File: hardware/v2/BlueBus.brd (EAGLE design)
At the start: 95 x 65 mm, 136 parts, among them J1 3PIN_953442_1, J2 6PIN_953442_1, J3 6PIN_5_103166_1, J4 SJ2-35853A-SMT-TR, J5 SMB_CONN, J6 USB3080-30-01-A, J7 PCM12SMTR, J8 TC2030, Q1 NMOSFET-BSS138K, Q2 PMOSFET-DMP32D4SSOT323, Q3 NMOSFET-BSS138K, U1 MPQ4420, U10 PCM5122, U11 PAM8406, U2 TH3122.4, U3 FT231XS, U4 S-1212BC0-U5T1U, U5 XC6210, U6 CAT25M01, U7 PIC24FJ1024GA606, U8 BM83SM1, U9 DIT4096

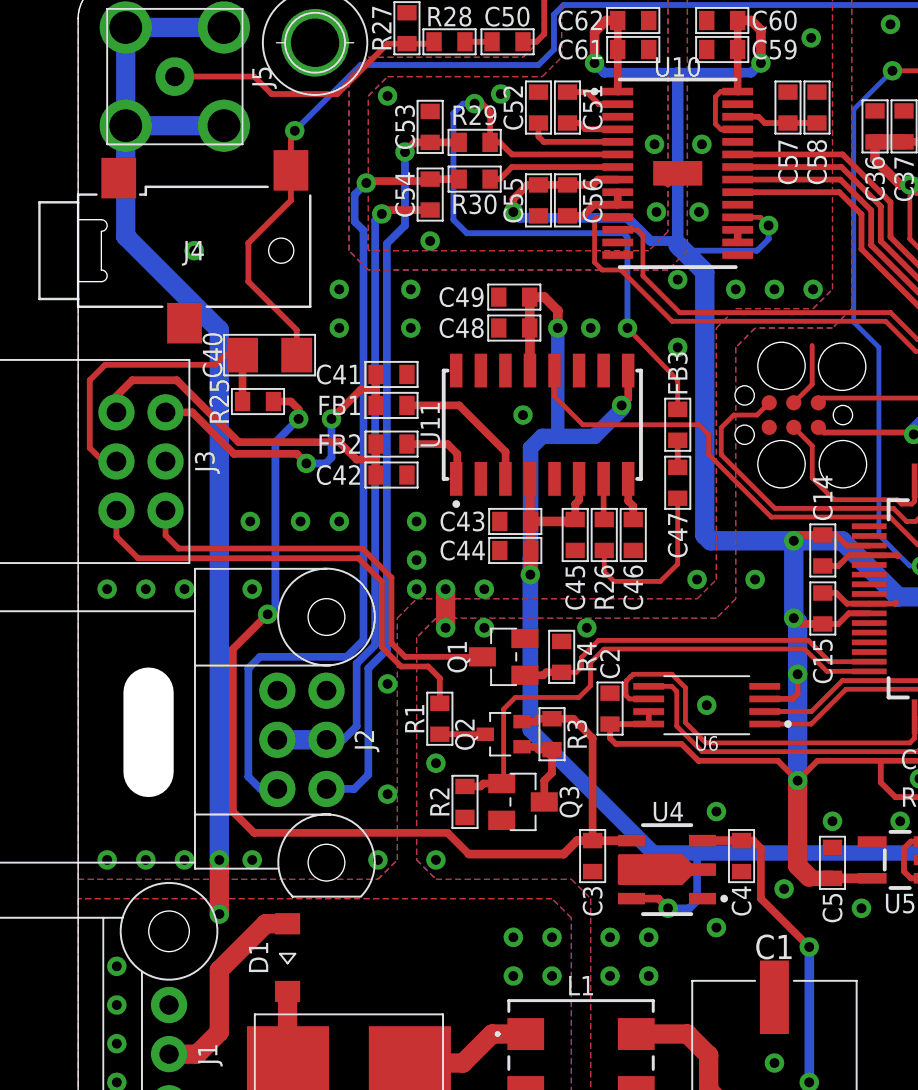
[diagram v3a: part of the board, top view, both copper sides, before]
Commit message: [IMP] hardware: V2 wiring and names * Update GND_FLT trace routing away from board cutout * Fix >NAME for some parts
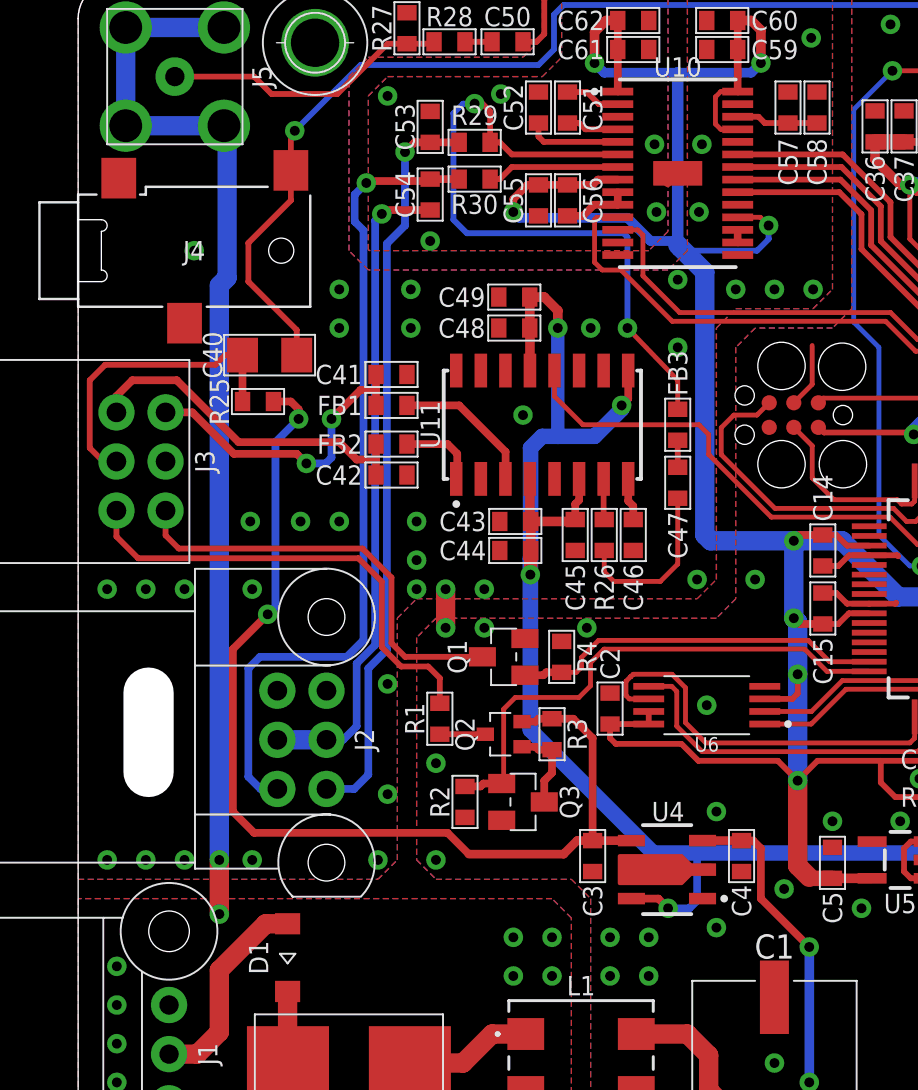
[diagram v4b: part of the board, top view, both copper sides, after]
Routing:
- net GND_FLT: track 58.0 -> 56.2 mm
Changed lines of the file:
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@@
 <element name="C1" library="Passives" package="RHS1V101MCN1GS" value="RHS1V101MCN1GS" x="36" y="9" smashed="yes" rot="R90">
 <attribute name="MFG" value="Nichicon" x="90.61" y="26.78" size="1.778" layer="27" rot="R90" display="off"/>
-<attribute name="NAME" x="36" y="15" size="1.25" layer="25" font="vector" ratio="15" rot="SR0" align="center"/>
+<attribute name="NAME" x="36" y="14.4" size="1.25" layer="25" font="vector" ratio="15" rot="SR0" align="bottom-center"/>
 <attribute name="PN" value="RHS1V101MCN1GS" x="90.61" y="26.78" size="1.778" layer="27" rot="R90" display="off"/>
 </element>
@@
 <element name="U6" library="ICs" package="TSSOP-8" value="CAT25M01" x="32.5" y="27.5" smashed="yes" rot="R180">
 <attribute name="MFG" value="ONSEMI" x="32.5" y="27.5" size="1.778" layer="27" rot="R180" display="off"/>
-<attribute name="NAME" x="32.5" y="25.9" size="0.75" layer="21" font="vector" ratio="15" rot="R180" align="bottom-center"/>
+<attribute name="NAME" x="32.5" y="25.85" size="0.75" layer="21" font="vector" ratio="15" rot="R180" align="bottom-center"/>
 <attribute name="PN" value="CAT25M01YI-GT3" x="32.5" y="27.5" size="1.778" layer="27" rot="R180" display="off"/>
 </element>
@@
 <wire x1="2.46" y1="62.54" x2="2.46" y2="57.46" width="1" layer="16"/>
 <wire x1="2.46" y1="57.46" x2="7.54" y2="57.46" width="1" layer="16"/>
-<wire x1="2.46" y1="57.46" x2="2.46" y2="51.74" width="1" layer="16"/>
-<wire x1="2.46" y1="51.74" x2="7.3" y2="46.9" width="1" layer="16"/>
 <via x="7.3" y="19.5" extent="1-16" drill="0.51"/>
-<wire x1="7.3" y1="46.9" x2="7.3" y2="19.5" width="1" layer="16"/>
 <via x="7.3" y="16.7" extent="1-16" drill="0.51"/>
 <wire x1="7.3" y1="19.5" x2="7.3" y2="16.7" width="1" layer="1"/>
+<wire x1="7.3" y1="49.2" x2="7.7" y2="49.6" width="1" layer="16"/>
+<wire x1="7.7" y1="49.6" x2="7.7" y2="57.3" width="1" layer="16"/>
+<wire x1="7.7" y1="57.3" x2="7.54" y2="57.46" width="1" layer="16"/>
+<wire x1="7.3" y1="19.5" x2="7.3" y2="49.2" width="1" layer="16"/>
+<wire x1="22.5" y1="15.5" x2="24.5" y2="15.5" width="0" layer="19" extent="1-1"/>
+<wire x1="24.5" y1="13.5" x2="24.5" y2="15.5" width="0" layer="19" extent="1-1"/>
+<wire x1="22.5" y1="13.5" x2="22.5" y2="15.5" width="0" layer="19" extent="1-1"/>
+<wire x1="23.1425" y1="7.5" x2="22.5" y2="13.5" width="0" layer="19" extent="1-1"/>
+<wire x1="22.5" y1="5" x2="23.1425" y2="7.5" width="0" layer="19" extent="1-1"/>
+<wire x1="22.5" y1="3.2" x2="22.5" y2="5" width="0" layer="19" extent="1-1"/>
+<wire x1="24.5" y1="5" x2="22.5" y2="5" width="0" layer="19" extent="1-1"/>
+<wire x1="24.5" y1="3.2" x2="24.5" y2="5" width="0" layer="19" extent="1-1"/>
+<wire x1="24.5" y1="1" x2="24.5" y2="3.2" width="0" layer="19" extent="1-1"/>
+<wire x1="22.5" y1="1" x2="24.5" y2="1" width="0" layer="19" extent="1-1"/>
+<wire x1="12.25" y1="3.25" x2="22.5" y2="3.2" width="0" layer="19" extent="1-1"/>
+<wire x1="2" y1="6" x2="12.25" y2="3.25" width="0" layer="19" extent="1-1"/>
+<wire x1="2" y1="8" x2="2" y2="6" width="0" layer="19" extent="1-1"/>
+<wire x1="2" y1="10" x2="2" y2="8" width="0" layer="19" extent="1-1"/>
+<wire x1="2" y1="12" x2="2" y2="10" width="0" layer="19" extent="1-1"/>
+<wire x1="2" y1="14" x2="2" y2="12" width="0" layer="19" extent="1-1"/>
+<wire x1="4.7" y1="12" x2="2" y2="12" width="0" layer="19" extent="1-1"/>
+<wire x1="7.3" y1="16.7" x2="4.7" y2="12" width="0" layer="19" extent="1-1"/>
 </signal>
 <signal name="MCU_VER">

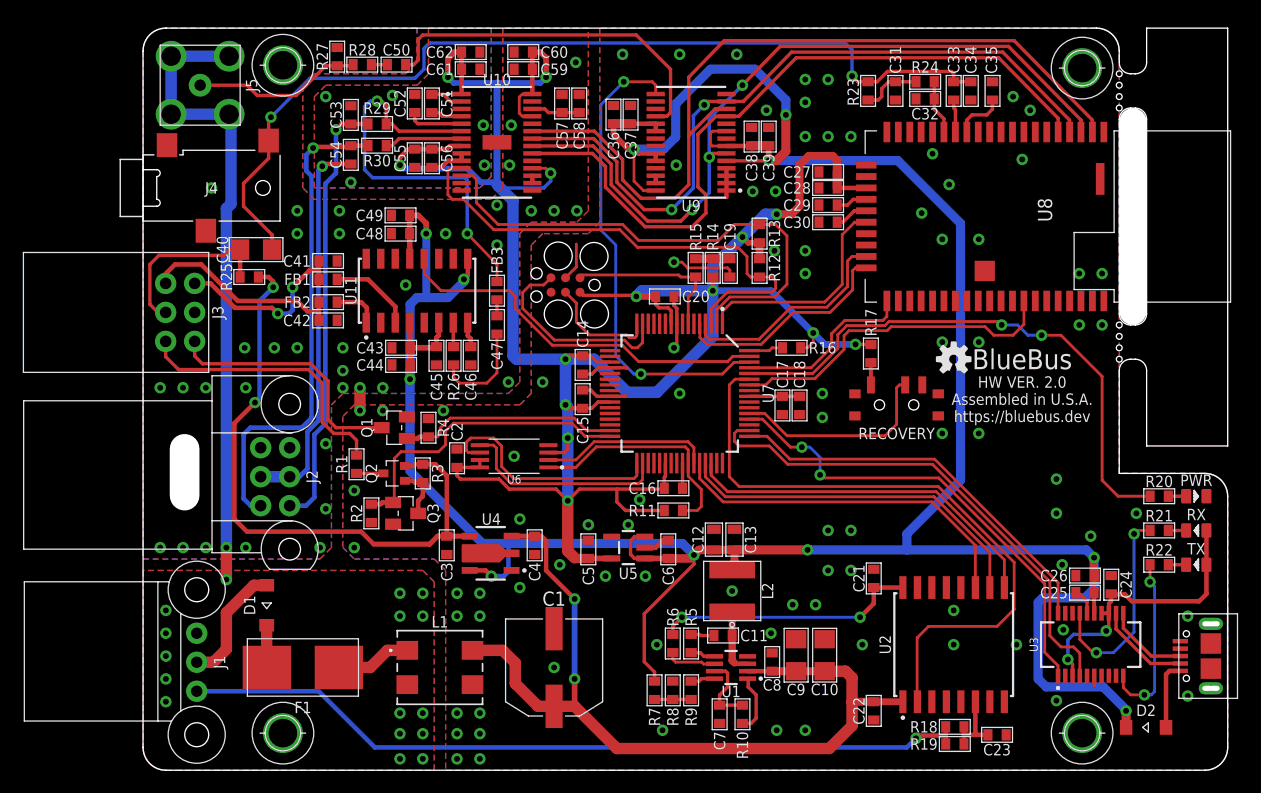
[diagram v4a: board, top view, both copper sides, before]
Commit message: [IMP] hardware: v2.0 TEL Circuit * Add Series resistor and move MOSFETs and resistors around to support BJT usage
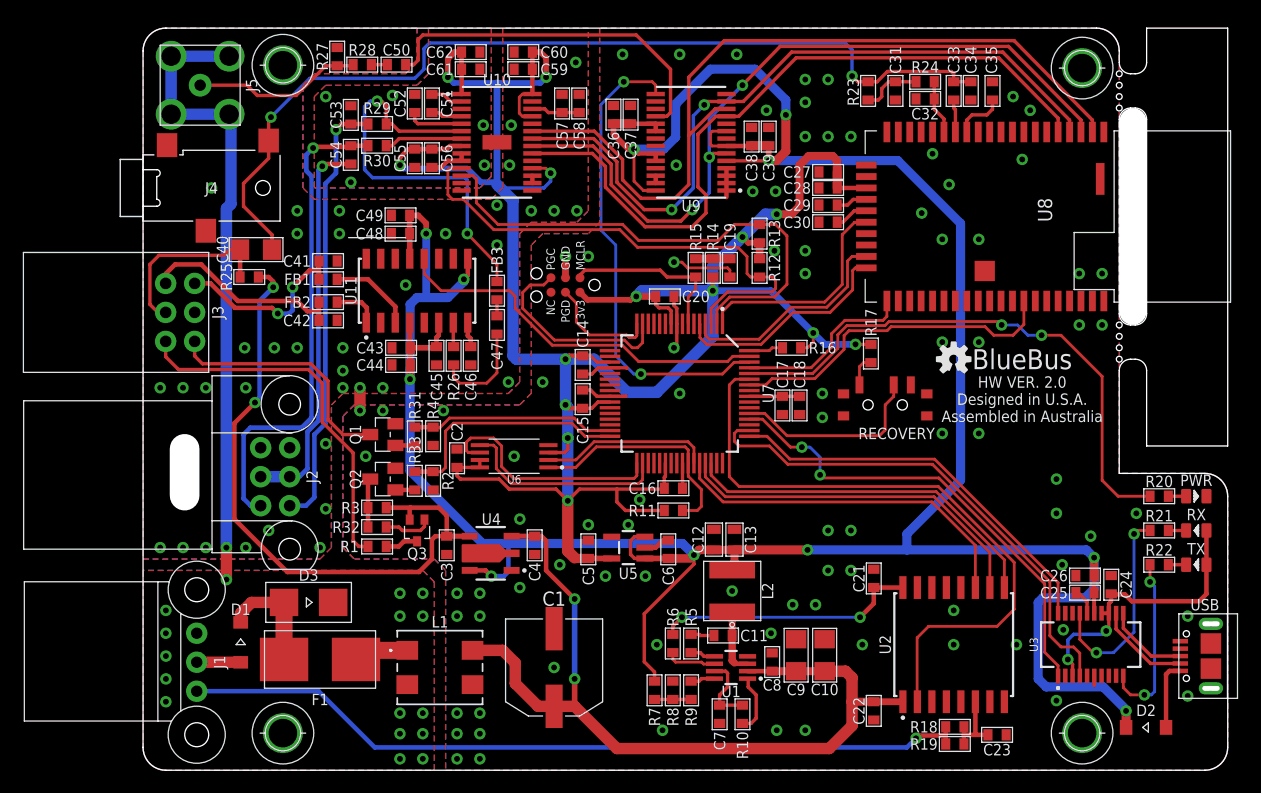
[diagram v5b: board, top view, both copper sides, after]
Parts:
- added D3: SMBJ18A, Passives:DO-214AA
- added R31, R32, R33: 1k, Passives:0603
- J8: value TC2030 -> TC2030NL; device Connectors:TC2030 -> Connectors:TC2030-NL
- Q2: value PMOSFET-DMP32D4SSOT323 -> NMOSFET-BSS138K; device Passives:SOT323 -> Passives:SOT-23
- Q3: value NMOSFET-BSS138K -> PMOSFET-DMP32D4SSOT323; device Passives:SOT-23 -> Passives:SOT323
- moved R1 7.42 mm to (20.5, 19.6), turned to 180 degrees
- moved R2 6.11 mm to (25.4, 25.4)
- moved R3 5.00 mm to (20.5, 23.0), turned to 0 degrees
- moved D1 3.97 mm to (8.55, 11.2), turned to 270 degrees
- moved Q3 1.80 mm to (24.0, 21.0), turned to 180 degrees
- moved F1 1.66 mm to (15.5, 9.70)
- moved Q1 1.17 mm to (21.0, 29.4)
- moved Q2 1.12 mm to (21.0, 25.5)
- moved J7 1.00 mm to (65.0, 32.0)
- moved R4 0.85 mm to (25.4, 29.2)
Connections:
- removed net TEL_ON_EN: Q2.1, Q3.3, R3.1
- new net MCU_TEL_MUTE_RES: Q1.1, R31.2
- new net MCU_TEL_ON_NRES: Q2.1, R33.2
- new net TEL_ON_P: Q2.3, R3.1, R32.1
- new net TEL_ON_P_RES: Q3.1, R32.2
- net 12V: now also Q3.2; no longer Q2.2
- net GND: now also Q2.2, R4.2; no longer Q3.2, R4.1
- net GND_FLT: now also D3.A
- net MCU_TEL_MUTE: now also R31.1, R4.1; no longer Q1.1, R4.2
- net MCU_TEL_ON: now also R33.1; no longer Q3.1
- net TEL_ON: now also Q3.3; no longer Q2.3
- net VBAT_DIODE: now also D3.C
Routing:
- net TEL_ON_IO: track 24.4 -> 32.4 mm
- net VBAT: track 10.8 -> 3.85 mm
- net VBAT_DIODE: track 3.71 -> 9.99 mm
- net MCU_TEL_ON: track 27.2 -> 21.2 mm
- net TEL_ON_EN: track 4.48 -> 0.00 mm
- net TEL_ON_P: track 0.00 -> 4.28 mm
- net TEL_ON_P_RES: track 0.00 -> 4.22 mm
- net 12V: track 54.9 -> 57.0 mm
- net VBAT_FLT: track 6.61 -> 4.82 mm
- net MCU_TEL_ON_NRES: track 0.00 -> 1.70 mm
- net MCU_TEL_MUTE_RES: track 0.00 -> 1.70 mm
- net GND: track 35.6 -> 34.1 mm, vias 123 -> 125
- net MCU_TEL_MUTE: track 19.3 -> 17.9 mm
- net MCU_RECOVERY: track 18.2 -> 17.2 mm
- net RECOVERY_ON: track 1.95 -> 2.74 mm
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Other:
- board text added: "3v3"
- board text added: "AGND"
- board text added: "Assembled in Australia"
- board text added: "Designed in U.S.A."
- board text added: "GND"
- board text added: "I/K-BUS"
- board text added: "MCLR"
- board text added: "MIC IN"
- board text added: "MIC+"
- board text added: "MIC-"
- board text added: "NC"
- board text added: "OUT_L"
- board text added: "OUT_R"
- board text added: "PGC"
- board text added: "PGD"
- board text added: "S/PDIF"
- board text added: "TEL_MUTE"
- board text added: "TEL_ON"
- board text added: "TEL_OUT+"
- board text added: "TEL_OUT-"
- board text added: "USB"
- board text added: "VIN"
- board text removed: "Assembled in U.S.A."
- board text removed: "https://bluebus.dev"

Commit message: [IMP] hardware: v2.0 Silkscreen * Update Bottom Silkscreen * Renumber Resistors
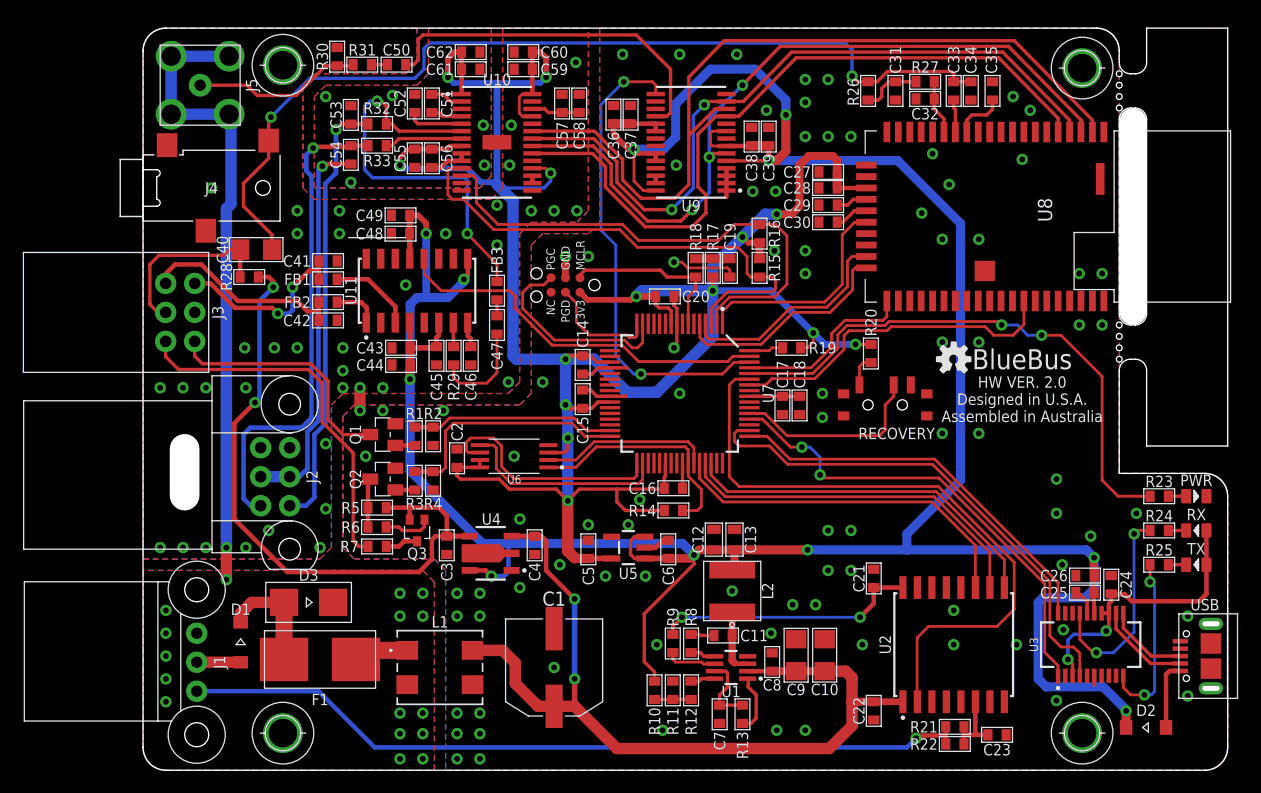
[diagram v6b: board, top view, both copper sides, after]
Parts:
- R1: value 4.7k -> 1k
- R10: value 100k -> 41.2k
- R11: value 4.7k -> 7.68k
- R12: value 4.7k -> 51k
- R13: value 4.7k -> 100k
- R14, R16: value 10k -> 4.7k
- R15: value 150 -> 4.7k
- R18: value 20 -> 150
- R19, R5: value 20 -> 10k
- R20: value 2k -> 10k
- R21, R22: value 2k -> 20
- R23, R24: value 1k -> 2k
- R25: value 10k -> 2k
- R26: value 18k -> 1k
- R27: value 150 -> 1k
- R28: value 150 -> 10k
- R29: value 100 -> 18k
- R3: value 10k -> 1k
- R30: value 100 -> 150
- R31: value 1k -> 150
- R32, R33: value 1k -> 100
- R6: value 100k -> 1k
- R7: value 41.2k -> 4.7k
- R8: value 7.68k -> 20
- R9: value 51k -> 100k
- moved R25 83.6 mm to (89.0, 18.0)
- moved R27 51.5 mm to (68.5, 60.3), turned to 0 degrees
- moved R18 46.2 mm to (48.4, 44.0), turned to 270 degrees
- moved R24 44.3 mm to (89.0, 21.0), turned to 180 degrees
- moved R23 43.7 mm to (89.0, 24.0), turned to 180 degrees
- moved R26 43.1 mm to (63.5, 59.5), turned to 270 degrees
- moved R13 42.1 mm to (52.5, 4.90), turned to 90 degrees
- moved R19 37.5 mm to (56.8, 37.0)
- moved R12 37.5 mm to (48.0, 7.00)
- moved R32 35.3 mm to (20.5, 56.6), turned to 180 degrees
- moved R31 32.9 mm to (19.2, 61.8), turned to 180 degrees
- moved R5 30.0 mm to (20.5, 23.0), turned to 0 degrees
- moved R33 29.5 mm to (20.5, 54.7), turned to 180 degrees
- moved R20 28.2 mm to (63.8, 36.5), turned to 90 degrees
- moved R6 27.8 mm to (20.5, 21.3), turned to 0 degrees
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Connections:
- net 12V: now also R28.1, R5.2; no longer R25.1, R3.2
- net 3.3V: now also R14.2, R15.2, R17.1, R19.2, R20.2; no longer R11.2, R12.2, R13.2, R14.1, R17.2
- net 5V: now also R10.2; no longer R7.2
- net 5VREG_BS: now also R8.1; no longer R5.1
- net 5VREG_BS_CAP: now also R8.2; no longer R5.2
- net 5VREG_EN: now also R9.1; no longer R6.1
- net 5VREG_FB: now also R12.2; no longer R9.2
- net 5VREG_FB_T: now also R10.1, R11.2, R12.1; no longer R7.1, R8.2, R9.1
- net 5VREG_PG: now also R13.1; no longer R10.1
- net 5VREG_VCC: now also R13.2; no longer R10.2
- net BT_MIC_L: now also R26.1; no longer R23.1
- net DAC_OUT_L: now also R32.1; no longer R29.1
- net DAC_OUT_R: now also R33.1; no longer R30.1
- net EE_CS: now also R14.1; no longer R11.1
- net GND: now also R11.1, R2.2, R30.2, R4.1; no longer R2.1, R27.2, R4.2, R8.1
- net IBUS: now also R21.1, R22.1; no longer R18.1, R19.1
- net IBUS_5V: now also R9.2; no longer R6.2
- net IBUS_FILT: now also R21.2, R22.2; no longer R18.2, R19.2
- net MCU_MCLR: now also R18.2; no longer R15.2
- net MCU_MCLR_RES: now also R17.2, R18.1; no longer R14.2, R15.1
- net MCU_ON_LED: now also R23.2; no longer R20.2
- net MCU_ON_LED_RES: now also R23.1; no longer R20.1
- net MCU_SCK3: now also R16.1; no longer R13.1
- net MCU_SDA3: now also R15.1; no longer R12.1
- net MCU_TEL_MUTE: now also R1.1, R2.1; no longer R31.1, R4.1
- net MCU_TEL_MUTE_RES: now also R1.2; no longer R31.2
- net MCU_TEL_ON: now also R3.1, R4.2; no longer R2.2, R33.1
- net MCU_TEL_ON_NRES: now also R3.2; no longer R33.2
- net MCU_VER: now also R19.1; no longer R16.1
- net MICP1_RES: now also R26.2, R27.1; no longer R23.2, R24.1
- net MIC_BIAS: now also R27.2; no longer R24.2
- net RECOVERY_ON: now also R20.1; no longer R17.1
- net SPDIF_OUT: now also R30.1, R31.2; no longer R27.1, R28.2
- net SPDIF_TX_RES: now also R31.1; no longer R28.1
- net SPKR_OUT_L: now also R32.2; no longer R29.2
- net SPKR_OUT_R: now also R33.2; no longer R30.2
- net SYS_RX_LED: now also R24.2; no longer R21.2
- net SYS_RX_LED_RES: now also R24.1; no longer R21.1
- net SYS_TX_LED: now also R25.2; no longer R22.2
- net SYS_TX_LED_RES: now also R25.1; no longer R22.1
- net TEL_AMP_INL: now also R29.2; no longer R26.2
- net TEL_AMP_INL_CAP_RES: now also R29.1; no longer R26.1
- net TEL_MIC_L_OUT: now also R28.2; no longer R25.2
- net TEL_ON: now also R7.1; no longer R1.1
- net TEL_ON_IO: now also R7.2; no longer R1.2
- net TEL_ON_P: now also R5.1, R6.1; no longer R3.1, R32.1
- net TEL_ON_P_RES: now also R6.2; no longer R32.2
